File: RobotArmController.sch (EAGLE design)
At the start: 63 parts, among them M1 M02LOCK, M2 M02LOCK, M3 M02LOCK, M4 M02LOCK, M5 M02LOCK, M6 M02LOCK

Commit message: Route motor drivers
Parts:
- removed R1: (no value), tekdemo:RESISTORUNIVERSAL
- added RLED: (no value), tekdemo:RESISTORUNIVERSAL
- renumbered M6 to MLED
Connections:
- removed net GND_M6: R1.1, U$13.P$2
- removed net M1: U$M1B.OUT1
- removed net M10: U$M5B.OUT2
- removed net M2: U$M1B.OUT2
- removed net M3: U$M2B.OUT1
- removed net M4: U$M2B.OUT2
- removed net M5: U$M3B.OUT1
- removed net M6: U$M3B.OUT2
- removed net M7: U$M4B.OUT1
- removed net M8: U$M4B.OUT2
- removed net M9: U$M5B.OUT1
- new net GND_LED: RLED.1, U$13.P$2
- new net N$10: U$22.P$1
- new net N$11: U$23.P$1
- new net N$2: U$15.P$1
- new net N$3: U$14.P$1
- new net N$4: U$16.P$1
- new net N$5: U$17.P$1
- new net N$6: U$19.P$1
- new net N$7: U$18.P$1
- new net N$8: U$21.P$1
- new net N$9: U$20.P$1
- net N$1: now also MLED.1, RLED.2; no longer MLED.2, R1.2
- net T13/LED: now also MLED.2; no longer MLED.1
- net VM1A: now also U$M1B.OUT1
- net VM1B: now also U$M1B.OUT2
- net VM2A: now also U$M2B.OUT1
- net VM2B: now also U$M2B.OUT2
- net VM3A: now also U$M3B.OUT1
- net VM3B: now also U$M3B.OUT2
- net VM4A: now also U$M4B.OUT1
- net VM4B: now also U$M4B.OUT2
- net VM5A: now also U$M5B.OUT1
- net VM5B: now also U$M5B.OUT2

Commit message: Route + Define mechanical
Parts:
- removed BAT1, LIPO: 1x3 RA Female .1", tekdemo:M03SMD_RA_FEMALE
- added JP1: M02JST-PTH-2, tekdemo:M02JST-PTH-2
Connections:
- removed net N$10: U$22.P$1
- removed net N$11: U$23.P$1
- removed net N$2: U$15.P$1
- removed net N$3: U$14.P$1
- removed net N$4: U$16.P$1
- removed net N$5: U$17.P$1
- removed net N$6: U$19.P$1
- removed net N$7: U$18.P$1
- removed net N$8: U$21.P$1
- removed net N$9: U$20.P$1
- removed net T/6/PWM: U$12.6/PWM
- removed net VBAT: BAT1.3, U$4.P$1
- removed net VHALFBAT: BAT1.2
- new net T6/PWM: U$12.6/PWM, U$16.P$1
- net GND: now also JP1.1; no longer BAT1.1
- net GND_LED: now also MLED.1; no longer RLED.1
- net N$1: now also MLED.2; no longer MLED.1
- net T10/PWM: now also U$14.P$1
- net T13/LED: now also RLED.1; no longer MLED.2
- net T20/PWM: now also U$20.P$1
- net T21/PWM: now also U$21.P$1
- net T22/PWM: now also U$22.P$1
- net T23/PWM: now also U$23.P$1
- net T3/PWM: now also U$19.P$1
- net T4/PWM: now also U$18.P$1
- net T5/PWM: now also U$17.P$1
- net T9/PWM: now also U$15.P$1
- net VIN: now also JP1.2, U$4.P$1
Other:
- moved on the sheet: RLED

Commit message: Wire to teensy
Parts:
- added JP2, JP3, JP4, JP5, JP6: (no value), tekdemo:M03LOCK
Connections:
- new net 3.3V: JP2.2, JP3.2, JP4.2, JP5.2, JP6.2, U$12.3.3V
- net GND: now also JP2.1, JP3.1, JP4.1, JP5.1, JP6.1
- net T15/A1: now also JP3.3
- net T16/A2: now also JP4.3
- net T17/A3: now also JP5.3
- net T18/A4: now also JP6.3
- net T19/A5: now also JP2.3
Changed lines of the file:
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@@
 <part name="U$M1B" library="tekdemo" deviceset="ZXBM5210" device="SO8" value="ZXBM5210"/>
 <part name="JP1" library="tekdemo" deviceset="M02" device="JST-PTH-2"/>
+<part name="JP2" library="tekdemo" deviceset="M03" device="LOCK"/>
+<part name="JP3" library="tekdemo" deviceset="M03" device="LOCK"/>
+<part name="JP4" library="tekdemo" deviceset="M03" device="LOCK"/>
+<part name="JP5" library="tekdemo" deviceset="M03" device="LOCK"/>
+<part name="JP6" library="tekdemo" deviceset="M03" device="LOCK"/>
 </parts>
 <sheets>
@@
 <instance part="U$M1B" gate="G$1" x="83.82" y="27.94"/>
 <instance part="JP1" gate="G$1" x="-121.92" y="55.88"/>
+<instance part="JP2" gate="G$1" x="-116.84" y="-160.02"/>
+<instance part="JP3" gate="G$1" x="-116.84" y="-175.26"/>
+<instance part="JP4" gate="G$1" x="-116.84" y="-190.5"/>
+<instance part="JP5" gate="G$1" x="-116.84" y="-205.74"/>
+<instance part="JP6" gate="G$1" x="-116.84" y="-220.98"/>
 </instances>
 <busses>
@@
 <label x="-88.9" y="55.88" size="1.778" layer="95" xref="yes"/>
 <pinref part="JP1" gate="G$1" pin="1"/>
+</segment>
+<segment>
+<pinref part="JP6" gate="G$1" pin="1"/>
+<wire x1="-109.22" y1="-223.52" x2="-83.82" y2="-223.52" width="0.2032" layer="91"/>
+<wire x1="-83.82" y1="-223.52" x2="-83.82" y2="-208.28" width="0.2032" layer="91"/>
+<pinref part="JP5" gate="G$1" pin="1"/>
+<wire x1="-83.82" y1="-208.28" x2="-83.82" y2="-193.04" width="0.2032" layer="91"/>
+<wire x1="-83.82" y1="-193.04" x2="-83.82" y2="-177.8" width="0.2032" layer="91"/>
+<wire x1="-83.82" y1="-177.8" x2="-83.82" y2="-162.56" width="0.2032" layer="91"/>
+<wire x1="-83.82" y1="-162.56" x2="-83.82" y2="-157.48" width="0.2032" layer="91"/>
+<wire x1="-109.22" y1="-208.28" x2="-83.82" y2="-208.28" width="0.2032" layer="91"/>
+<pinref part="JP4" gate="G$1" pin="1"/>
+<wire x1="-109.22" y1="-193.04" x2="-83.82" y2="-193.04" width="0.2032" layer="91"/>
+<pinref part="JP3" gate="G$1" pin="1"/>
+<wire x1="-109.22" y1="-177.8" x2="-83.82" y2="-177.8" width="0.2032" layer="91"/>
+<pinref part="JP2" gate="G$1" pin="1"/>
+<wire x1="-109.22" y1="-162.56" x2="-83.82" y2="-162.56" width="0.2032" layer="91"/>
+<label x="-83.82" y="-157.48" size="1.778" layer="95" xref="yes"/>
 </segment>
 </net>
@@
 <label x="-119.38" y="-96.52" size="1.778" layer="95" rot="R180" xref="yes"/>
 </segment>
+<segment>
+<pinref part="JP2" gate="G$1" pin="3"/>
+<wire x1="-109.22" y1="-157.48" x2="-106.68" y2="-157.48" width="0.2032" layer="91"/>
+<label x="-106.68" y="-157.48" size="1.778" layer="95" xref="yes"/>
+</segment>
 </net>
 <net name="T18/A4" class="1">
@@
 <label x="-119.38" y="-93.98" size="1.778" layer="95" rot="R180" xref="yes"/>
 </segment>
+<segment>
+<pinref part="JP6" gate="G$1" pin="3"/>
+<wire x1="-109.22" y1="-218.44" x2="-106.68" y2="-218.44" width="0.2032" layer="91"/>
+<label x="-106.68" y="-218.44" size="1.778" layer="95" xref="yes"/>
+</segment>
 </net>
 <net name="T4/PWM" class="1">
@@
 <label x="-119.38" y="-91.44" size="1.778" layer="95" rot="R180" xref="yes"/>
 </segment>
+<segment>
+<pinref part="JP5" gate="G$1" pin="3"/>
+<wire x1="-109.22" y1="-203.2" x2="-106.68" y2="-203.2" width="0.2032" layer="91"/>
+<label x="-106.68" y="-203.2" size="1.778" layer="95" xref="yes"/>
+</segment>
 </net>
 <net name="T16/A2" class="1">
@@
 <label x="-119.38" y="-88.9" size="1.778" layer="95" rot="R180" xref="yes"/>
 </segment>
+<segment>
+<pinref part="JP4" gate="G$1" pin="3"/>
+<wire x1="-109.22" y1="-187.96" x2="-106.68" y2="-187.96" width="0.2032" layer="91"/>
+<label x="-106.68" y="-187.96" size="1.778" layer="95" xref="yes"/>
+</segment>
 </net>
 <net name="T15/A1" class="1">
@@
 <wire x1="-99.06" y1="-86.36" x2="-119.38" y2="-86.36" width="0.2032" layer="91"/>
 <label x="-119.38" y="-86.36" size="1.778" layer="95" rot="R180" xref="yes"/>
+</segment>
+<segment>
+<pinref part="JP3" gate="G$1" pin="3"/>
+<wire x1="-109.22" y1="-172.72" x2="-106.68" y2="-172.72" width="0.2032" layer="91"/>
+<label x="-106.68" y="-172.72" size="1.778" layer="95" xref="yes"/>
 </segment>
 </net>
@@
 </segment>
 </net>
+<net name="3.3V" class="0">
+<segment>
+<pinref part="JP6" gate="G$1" pin="2"/>
+<wire x1="-109.22" y1="-220.98" x2="-88.9" y2="-220.98" width="0.2032" layer="91"/>
+<wire x1="-88.9" y1="-220.98" x2="-88.9" y2="-205.74" width="0.2032" layer="91"/>
+<pinref part="JP5" gate="G$1" pin="2"/>
+<wire x1="-88.9" y1="-205.74" x2="-88.9" y2="-190.5" width="0.2032" layer="91"/>
+<wire x1="-88.9" y1="-190.5" x2="-88.9" y2="-175.26" width="0.2032" layer="91"/>
+<wire x1="-88.9" y1="-175.26" x2="-88.9" y2="-160.02" width="0.2032" layer="91"/>
+<wire x1="-88.9" y1="-160.02" x2="-88.9" y2="-152.4" width="0.2032" layer="91"/>
+<wire x1="-109.22" y1="-205.74" x2="-88.9" y2="-205.74" width="0.2032" layer="91"/>
+<pinref part="JP4" gate="G$1" pin="2"/>
+<wire x1="-109.22" y1="-190.5" x2="-88.9" y2="-190.5" width="0.2032" layer="91"/>
+<pinref part="JP3" gate="G$1" pin="2"/>
+<wire x1="-109.22" y1="-175.26" x2="-88.9" y2="-175.26" width="0.2032" layer="91"/>
+<pinref part="JP2" gate="G$1" pin="2"/>
+<wire x1="-109.22" y1="-160.02" x2="-88.9" y2="-160.02" width="0.2032" layer="91"/>
+<label x="-88.9" y="-152.4" size="1.778" layer="95" xref="yes"/>
+</segment>
+<segment>
+<pinref part="U$12" gate="G$1" pin="3.3V"/>
+<wire x1="-53.34" y1="-50.8" x2="-48.26" y2="-50.8" width="0.2032" layer="91"/>
+<label x="-48.26" y="-50.8" size="1.778" layer="95" xref="yes"/>
+</segment>
+</net>

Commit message: Adjust for silkscreen and labels
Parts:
- renumbered 0.1UF to M1C2, 0.1UF1 to M2C2, 0.1UF2 to M3C2, 0.1UF3 to M4C2, 0.1UF4 to M5C2, C1 to M1C4, C10 to M4C1, C11 to M4C3, C12 to M4C4, C13 to M5C1, C14 to M5C3, C15 to M5C4, C2 to M1C1, C3 to M1C3, C4 to M2C1, C5 to M2C3, C6 to M2C4, C7 to M3C1, C8 to M3C3, C9 to M3C4, JP2 to A5, JP3 to A1, JP4 to A2, JP5 to A3, JP6 to A4, MLED to LED, U$12 to TEENSY
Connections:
- removed net GND_LED: LED.1, U$13.P$2
- net GND: now also LED.1, U$13.P$2

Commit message: Remove LED resistor (not used)
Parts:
- removed RLED: (no value), tekdemo:RESISTORUNIVERSAL
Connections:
- removed net N$1: LED.2, RLED.2
- net T13/LED: now also LED.2; no longer RLED.1
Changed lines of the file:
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@@
 <part name="U$11" library="tekdemo" deviceset="NET-JUNCTION-2" device=""/>
 <part name="U$13" library="tekdemo" deviceset="NET-JUNCTION-2" device=""/>
-<part name="RLED" library="tekdemo" deviceset="RESISTOR" device="UNIVERSAL"/>
 <part name="LED" library="tekdemo" deviceset="M02" device="LOCK"/>
 <part name="TEENSY" library="Teensy_3_Series_Board_v1.0" deviceset="TEENSY_3.1_BASIC" device=""/>
@@
 <instance part="U$11" gate="G$1" x="17.78" y="-251.46"/>
 <instance part="U$13" gate="G$1" x="17.78" y="111.76"/>
-<instance part="RLED" gate="G$1" x="38.1" y="106.68"/>
 <instance part="LED" gate="G$1" x="55.88" y="111.76" rot="R180"/>
 <instance part="TEENSY" gate="G$1" x="-76.2" y="-76.2"/>
@@
 </segment>
 <segment>
-<wire x1="33.02" y1="106.68" x2="10.16" y2="106.68" width="0.2032" layer="91"/>
+<wire x1="43.18" y1="106.68" x2="10.16" y2="106.68" width="0.2032" layer="91"/>
 <label x="10.16" y="106.68" size="1.778" layer="95" rot="R180" xref="yes"/>
-<pinref part="RLED" gate="G$1" pin="1"/>
+<pinref part="LED" gate="G$1" pin="2"/>
+<wire x1="43.18" y1="106.68" x2="45.72" y2="109.22" width="0.2032" layer="91"/>
+<wire x1="45.72" y1="109.22" x2="48.26" y2="109.22" width="0.2032" layer="91"/>
 </segment>
 </net>
@@
 </segment>
 </net>
-<net name="N$1" class="1">
-<segment>
-<pinref part="LED" gate="G$1" pin="2"/>
-<wire x1="43.18" y1="106.68" x2="45.72" y2="109.22" width="0.2032" layer="91"/>
-<wire x1="45.72" y1="109.22" x2="48.26" y2="109.22" width="0.2032" layer="91"/>
-<pinref part="RLED" gate="G$1" pin="2"/>
-</segment>
-</net>

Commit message: Add OWI power connector, update gnd plane, silk
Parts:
- added JP2: M02LOCK, tekdemo:M02LOCK
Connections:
- net GND: now also JP2.1
- net VIN: now also JP2.2
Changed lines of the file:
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@@
 <part name="A3" library="tekdemo" deviceset="M03" device="LOCK"/>
 <part name="A4" library="tekdemo" deviceset="M03" device="LOCK"/>
+<part name="JP2" library="tekdemo" deviceset="M02" device="LOCK"/>
 </parts>
 <sheets>
@@
 <wire x1="-30.48" y1="76.2" x2="-132.08" y2="76.2" width="0.2032" layer="94" style="longdash"/>
 <text x="-132.08" y="78.74" size="1.778" layer="94">INPUT POWER</text>
-<text x="-124.46" y="50.8" size="1.778" layer="94" align="top-left">Note: During standard operation (with the controller),
+<text x="-124.46" y="38.1" size="1.778" layer="94" align="top-left">Note: During standard operation (with the controller),
 the batteries are used in a -3V/0V/+3V configuration
 </text>
@@
 <instance part="A3" gate="G$1" x="-116.84" y="-205.74"/>
 <instance part="A4" gate="G$1" x="-116.84" y="-220.98"/>
+<instance part="JP2" gate="G$1" x="-121.92" y="43.18"/>
 </instances>
 <busses>
@@
 <wire x1="-35.56" y1="33.02" x2="-40.64" y2="33.02" width="0.2032" layer="91"/>
 <label x="-40.64" y="33.02" size="1.778" layer="95" rot="R180" xref="yes"/>
+</segment>
+<segment>
+<pinref part="JP2" gate="G$1" pin="2"/>
+<wire x1="-114.3" y1="45.72" x2="-88.9" y2="45.72" width="0.2032" layer="91"/>
+<label x="-88.9" y="45.72" size="1.778" layer="95" xref="yes"/>
 </segment>
 </net>
@@
 <wire x1="22.86" y1="111.76" x2="48.26" y2="111.76" width="0.2032" layer="91"/>
 </segment>
-</net>
+<segment>
+<pinref part="JP2" gate="G$1" pin="1"/>
+<wire x1="-114.3" y1="43.18" x2="-88.9" y2="43.18" width="0.2032" layer="91"/>
+<label x="-88.9" y="43.18" size="1.778" layer="95" xref="yes"/>
+</segment>
+</net>

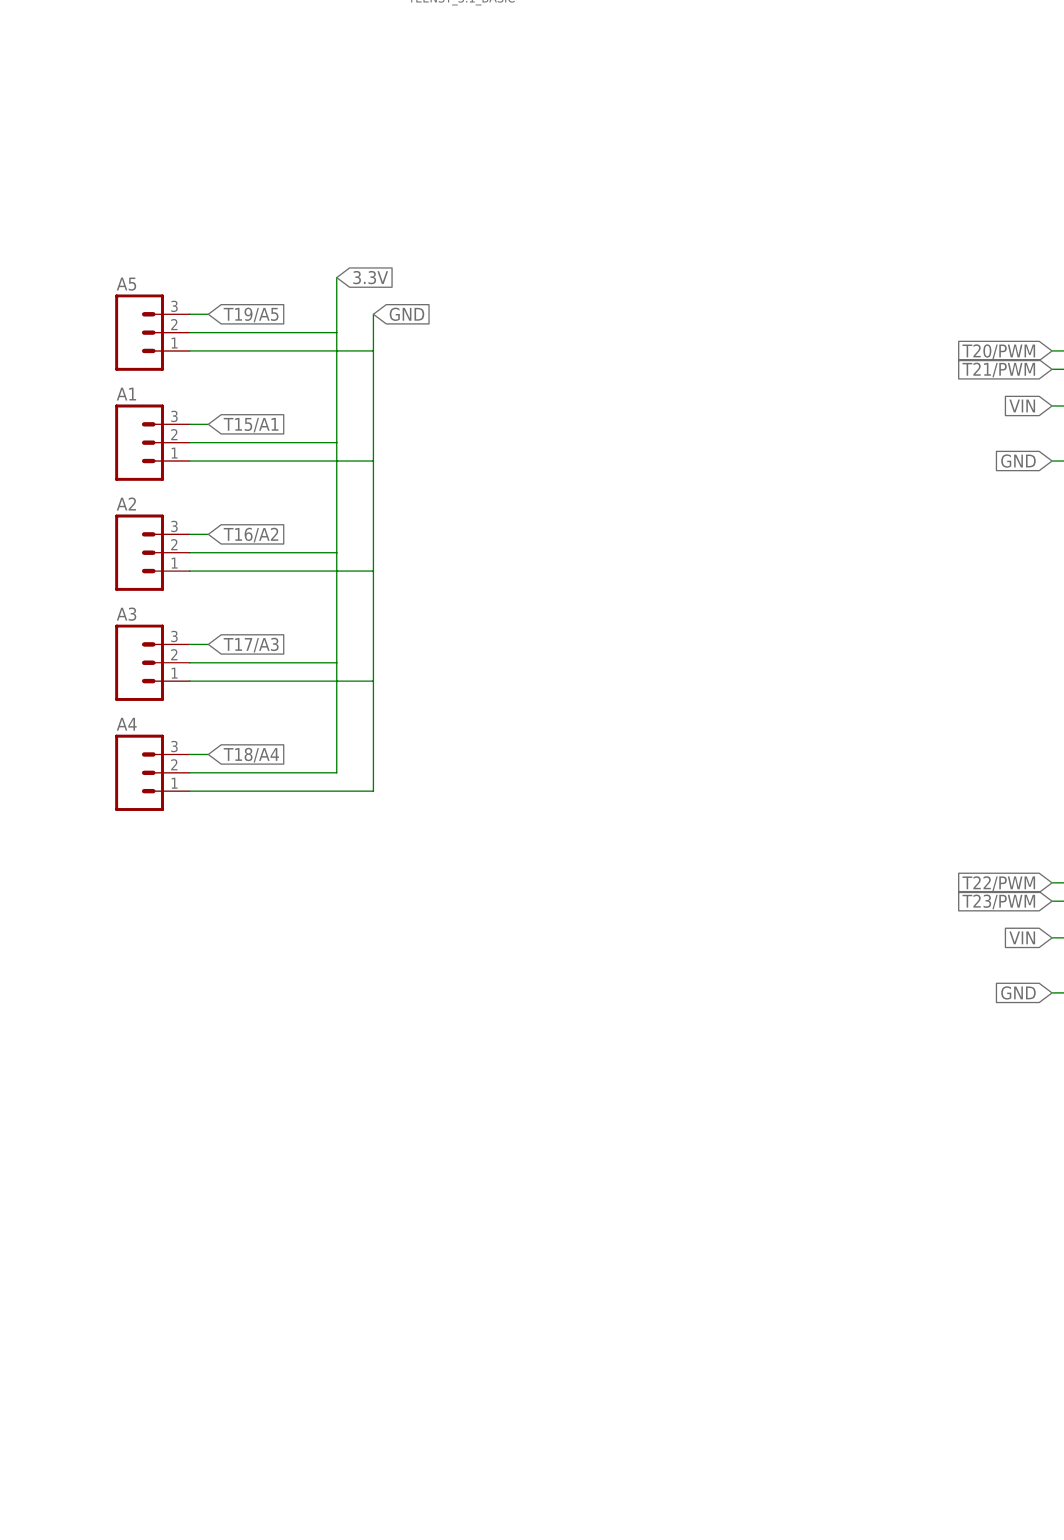
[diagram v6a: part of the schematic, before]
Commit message: Add controller input
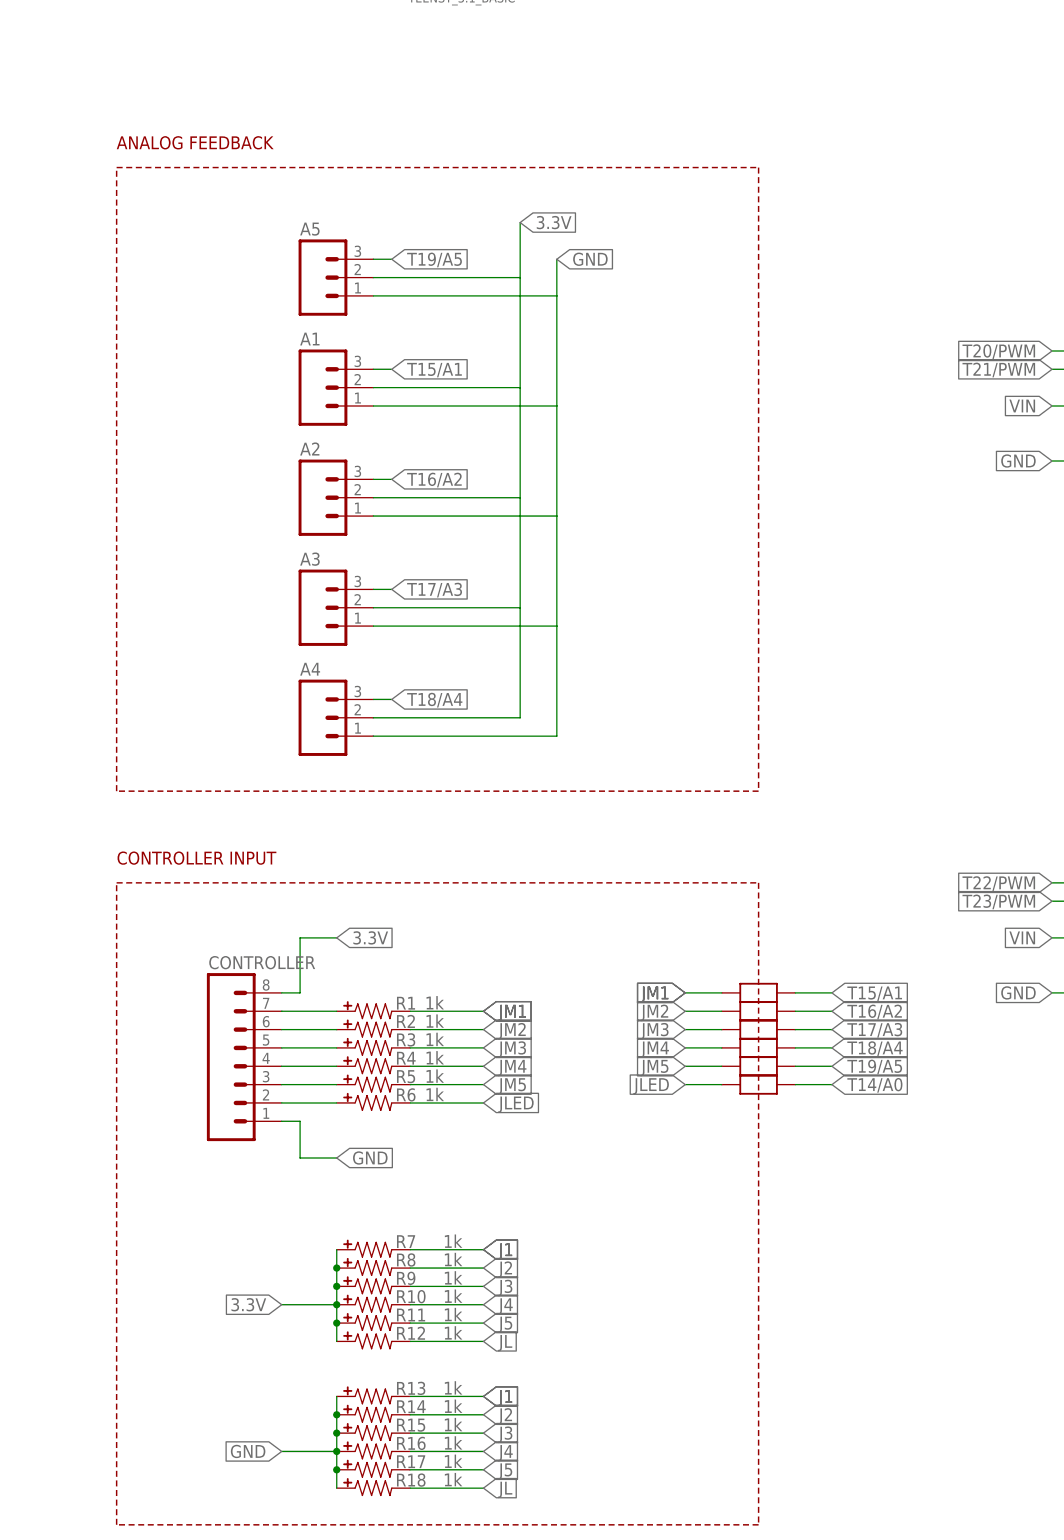
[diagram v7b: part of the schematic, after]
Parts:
- added CONTROLLER: (no value), SparkFun-Connectors:M08LOCK
- added R1, R10, R11, R12, R13, R14, R15, R16, R17, R18, R2, R3, R4, R5, R6, R7, R8, R9: 1k, tekdemo:RESISTORUNIVERSAL
- added U$12, U$25, U$26, U$27, U$28, U$29: NET-JUNCTION-2, tekdemo:NET-JUNCTION-2
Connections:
- new net J1: CONTROLLER.7, R1.1, R13.2, R7.2
- new net J2: CONTROLLER.6, R14.2, R2.1, R8.2
- new net J3: CONTROLLER.5, R15.2, R3.1, R9.2
- new net J4: CONTROLLER.4, R10.2, R16.2, R4.1
- new net J5: CONTROLLER.3, R11.2, R17.2, R5.1
- new net JL: CONTROLLER.2, R12.2, R18.2, R6.1
- new net JLED: R6.2, U$29.P$1
- new net JM1: R1.2, U$12.P$1
- new net JM2: R2.2, U$25.P$1
- new net JM3: R3.2, U$26.P$1
- new net JM4: R4.2, U$27.P$1
- new net JM5: R5.2, U$28.P$1
- net 3.3V: now also CONTROLLER.8, R10.1, R11.1, R12.1, R7.1, R8.1, R9.1
- net GND: now also CONTROLLER.1, R13.1, R14.1, R15.1, R16.1, R17.1, R18.1
- net T14/A0: now also U$29.P$2
- net T15/A1: now also U$12.P$2
- net T16/A2: now also U$25.P$2
- net T17/A3: now also U$26.P$2
- net T18/A4: now also U$27.P$2
- net T19/A5: now also U$28.P$2
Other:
- note added: "ANALOG FEEDBACK"
- note added: "CONTROLLER INPUT"
- moved on the sheet: A1, A2, A3, A4, A5
